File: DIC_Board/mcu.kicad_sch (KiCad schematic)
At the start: 1 part, among them U1 STM32L476ZGTx

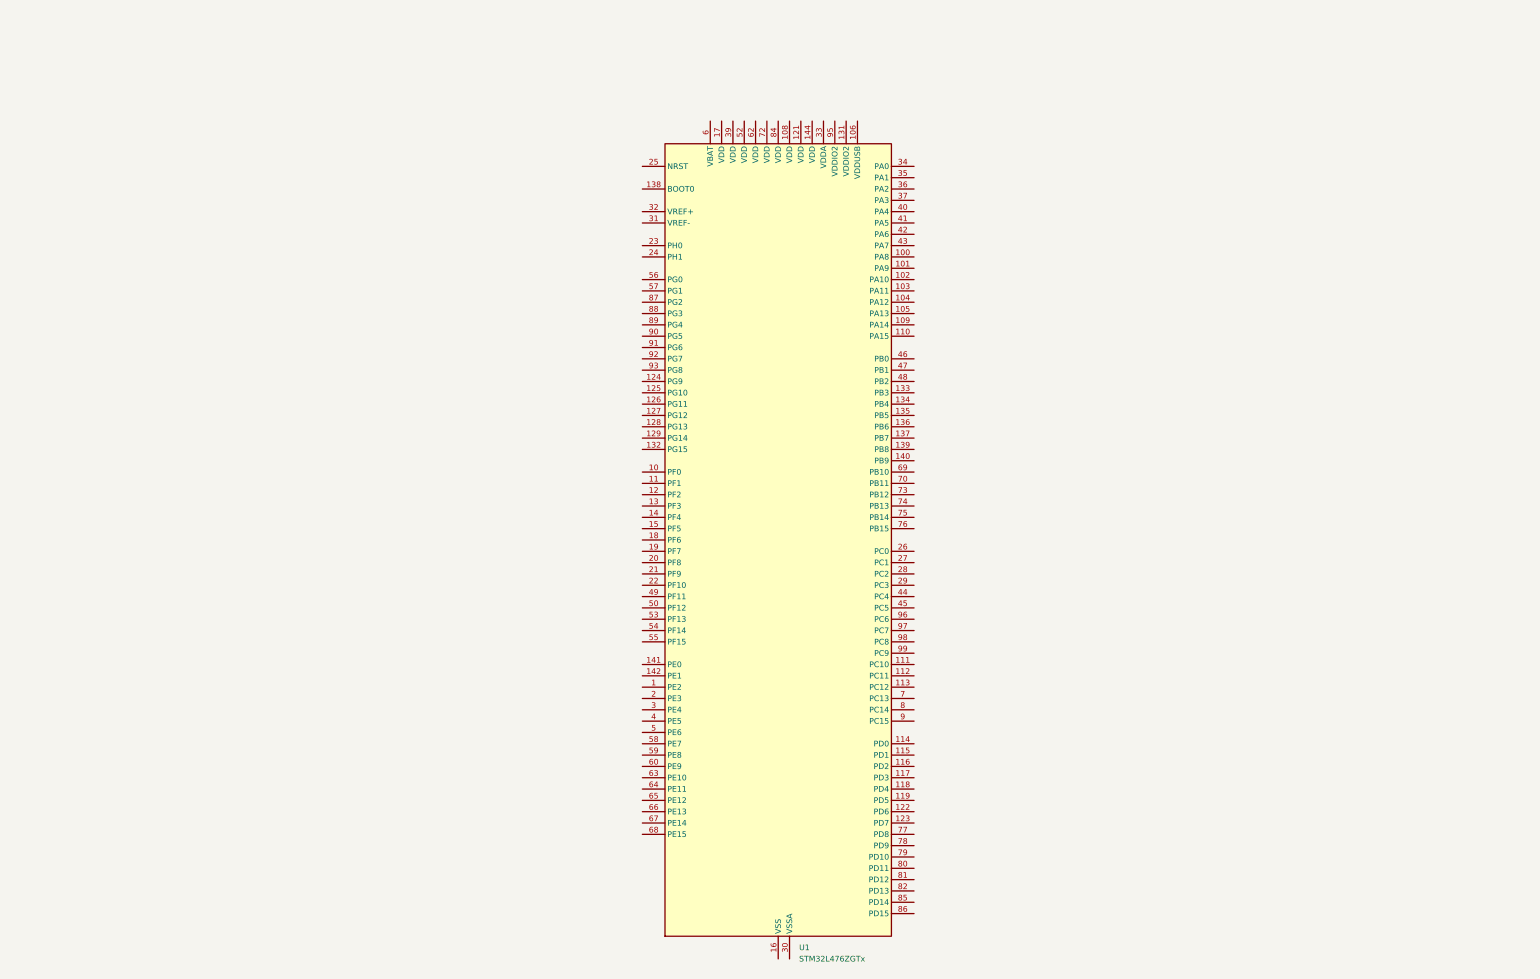
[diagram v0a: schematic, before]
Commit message: Add MCU schematic hierarchy and pin configuration
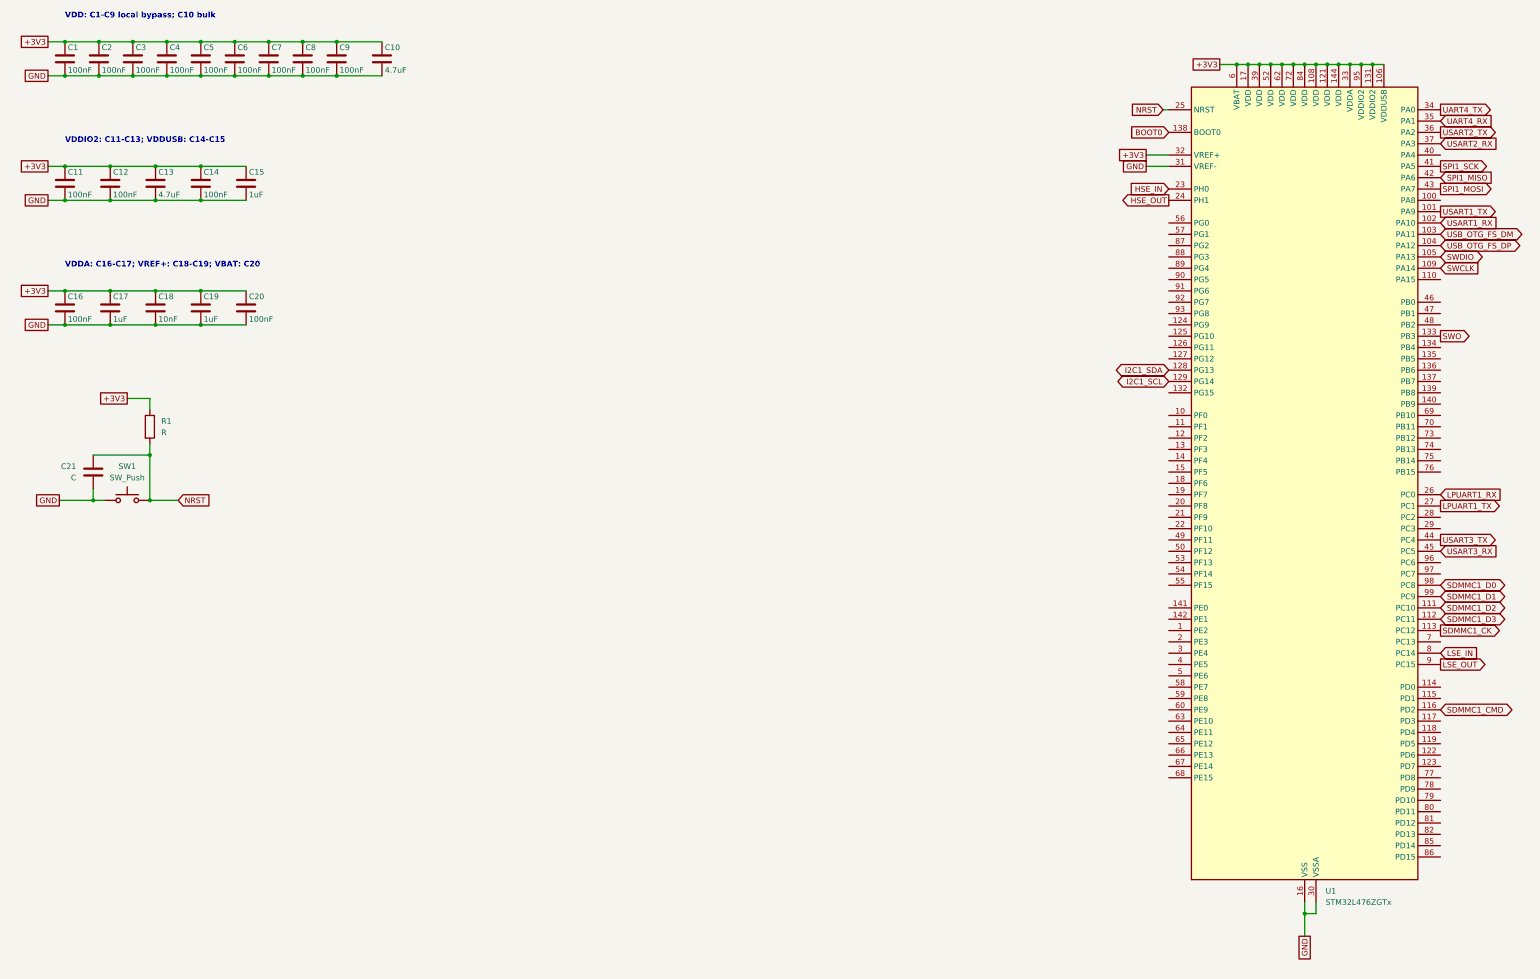
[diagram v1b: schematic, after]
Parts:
- added C1, C11, C12, C14, C16, C2, C20, C3, C4, C5, C6, C7, C8, C9: 100nF, Capacitor_SMD:C_0603_1608Metric, symbol Device:C
- added C10, C13: 4.7uF, Capacitor_SMD:C_0805_2012Metric, symbol Device:C
- added C15, C17, C19: 1uF, Capacitor_SMD:C_0603_1608Metric, symbol Device:C
- added C18: 10nF, Capacitor_SMD:C_0603_1608Metric, symbol Device:C
- added C21: C, symbol Device:C
- added R1: R, symbol Device:R
- added SW1: SW_Push, symbol Switch:SW_Push
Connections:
- net USART1_TX: now reaches U1.101 (PA9)
- net USART1_RX: now reaches U1.102 (PA10)
- net USB_OTG_FS_DM: now reaches U1.103 (PA11)
- net USB_OTG_FS_DP: now reaches U1.104 (PA12)
- net SWDIO: now reaches U1.105 (PA13)
- net +3V3: now reaches U1.106 (VDDUSB)
- net +3V3: now also U1.108 (VDD), U1.121 (VDD), U1.131 (VDDIO2), U1.144 (VDD), U1.17 (VDD), U1.32 (VREF+), U1.33 (VDDA), U1.39 (VDD), U1.52 (VDD), U1.6 (VBAT), U1.62 (VDD), U1.72 (VDD), U1.84 (VDD), U1.95 (VDDIO2), C1.1, C10.1, C11.1, C12.1, C13.1, C14.1, C15.1, C16.1, C17.1, C18.1, C19.1, C2.1, C20.1, C3.1, C4.1, C5.1, C6.1, C7.1, C8.1, C9.1, R1.1
- net GND: now reaches U1.107 (VSS), U1.120 (VSS), U1.130 (VSS), U1.143 (VSS), U1.16 (VSS), U1.38 (VSS), U1.51 (VSS), U1.61 (VSS), U1.71 (VSS), U1.83 (VSS), U1.94 (VSS)
- net GND: now also U1.30 (VSSA), U1.31 (VREF-), C1.2, C10.2, C11.2, C12.2, C13.2, C14.2, C15.2, C16.2, C17.2, C18.2, C19.2, C2.2, C20.2, C21.1, C3.2, C4.2, C5.2, C6.2, C7.2, C8.2, C9.2, SW1.1
- net SWCLK: now reaches U1.109 (PA14)
- net SDMMC1_D2: now reaches U1.111 (PC10)
- net SDMMC1_D3: now reaches U1.112 (PC11)
- net SDMMC1_CK: now reaches U1.113 (PC12)
- net SDMMC1_CMD: now reaches U1.116 (PD2)
- net I2C1_SDA: now reaches U1.128 (PG13)
- net I2C1_SCL: now reaches U1.129 (PG14)
- net SWO: now reaches U1.133 (PB3)
- net BOOT0: now reaches U1.138 (BOOT0)
- net HSE_IN: now reaches U1.23 (PH0)
- net HSE_OUT: now reaches U1.24 (PH1)
- net NRST: now reaches U1.25 (NRST)
- net NRST: now also C21.2, R1.2, SW1.2
- net LPUART1_RX: now reaches U1.26 (PC0)
- net LPUART1_TX: now reaches U1.27 (PC1)
- net UART4_TX: now reaches U1.34 (PA0)
- net UART4_RX: now reaches U1.35 (PA1)
- net USART2_TX: now reaches U1.36 (PA2)
- net USART2_RX: now reaches U1.37 (PA3)
- net SPI1_SCK: now reaches U1.41 (PA5)
- net SPI1_MISO: now reaches U1.42 (PA6)
- net SPI1_MOSI: now reaches U1.43 (PA7)
- net USART3_TX: now reaches U1.44 (PC4)
- net USART3_RX: now reaches U1.45 (PC5)
- net LSE_IN: now reaches U1.8 (PC14)
- net LSE_OUT: now reaches U1.9 (PC15)
- net SDMMC1_D0: now reaches U1.98 (PC8)
- net SDMMC1_D1: now reaches U1.99 (PC9)
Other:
- note added: "VDD: C1-C9 local bypass; C10 bulk"
- note added: "VDDA: C16-C17; VREF+: C18-C19; VBAT: C20"
- note added: "VDDIO2: C11-C13; VDDUSB: C14-C15"
- moved on the sheet: U1

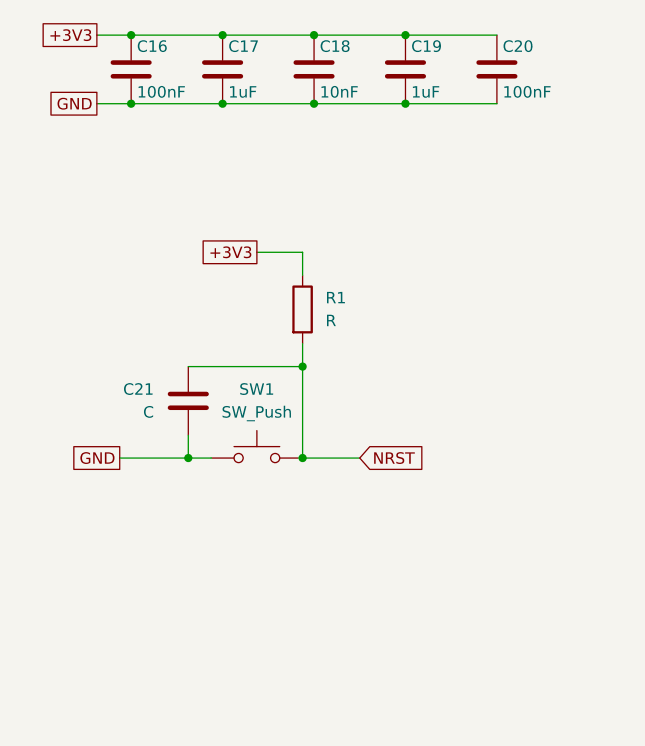
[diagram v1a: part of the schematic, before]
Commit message: Update MCU schematic and add project document
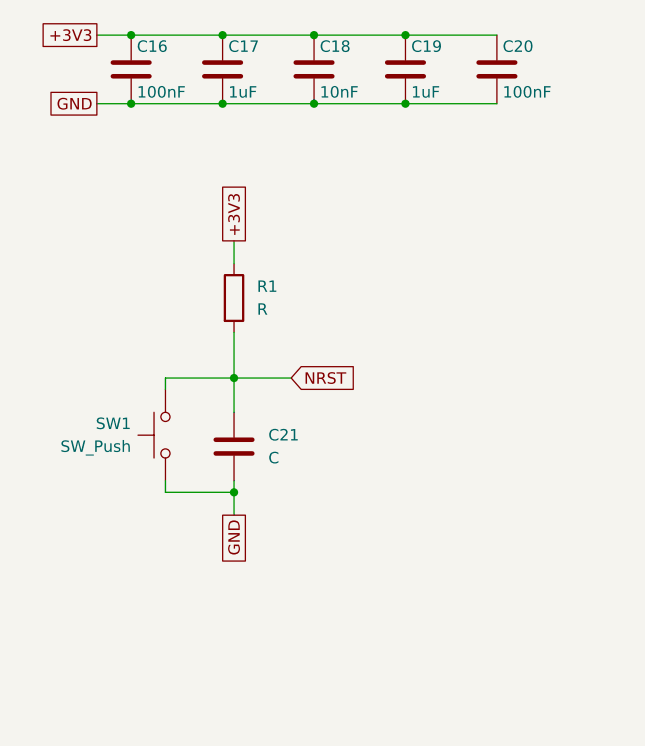
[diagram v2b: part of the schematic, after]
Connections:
- net GND: now also SW1.2; no longer SW1.1
- net NRST: now also SW1.1; no longer SW1.2
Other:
- moved on the sheet: C21, R1, SW1
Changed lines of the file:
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@@
 	)
 	(junction
-		(at 48.26 123.19)
-		(diameter 0)
-		(color 0 0 0 0)
-	)
-	(junction
 		(at 29.21 30.48)
 		(diameter 0)
@@
 	)
 	(junction
-		(at 29.21 38.1)
+		(at 40.64 137.16)
 		(diameter 0)
 		(color 0 0 0 0)
 	)
 	(junction
-		(at 35.56 133.35)
+		(at 29.21 38.1)
 		(diameter 0)
 		(color 0 0 0 0)
 	)
 	(junction
-		(at 48.26 133.35)
+		(at 40.64 124.46)
 		(diameter 0)
 		(color 0 0 0 0)
@@
 	(wire
 		(pts
-			(xy 35.56 130.81) (xy 35.56 133.35)
+			(xy 40.64 135.89) (xy 40.64 137.16)
 		)
 		(stroke
@@
 	(wire
 		(pts
-			(xy 43.18 110.49) (xy 48.26 110.49)
+			(xy 292.1 35.56) (xy 325.12 35.56)
 		)
 		(stroke
@@
 	(wire
 		(pts
-			(xy 292.1 35.56) (xy 325.12 35.56)
+			(xy 40.64 109.22) (xy 40.64 111.76)
 		)
 		(stroke
@@
 	(wire
 		(pts
-			(xy 48.26 110.49) (xy 48.26 113.03)
+			(xy 29.21 66.04) (xy 69.85 66.04)
 		)
 		(stroke
@@
 	(wire
 		(pts
-			(xy 29.21 66.04) (xy 69.85 66.04)
+			(xy 307.34 226.06) (xy 309.88 226.06)
 		)
 		(stroke
@@
 	(wire
 		(pts
-			(xy 307.34 226.06) (xy 309.88 226.06)
+			(xy 33.02 124.46) (xy 40.64 124.46)
 		)
 		(stroke
@@
 	(wire
 		(pts
-			(xy 35.56 123.19) (xy 48.26 123.19)
+			(xy 29.21 58.42) (xy 69.85 58.42)
 		)
 		(stroke
@@
 	(wire
 		(pts
-			(xy 29.21 58.42) (xy 69.85 58.42)
+			(xy 33.02 124.46) (xy 33.02 125.73)
 		)
 		(stroke
@@
 	(wire
 		(pts
-			(xy 29.21 30.48) (xy 100.33 30.48)
+			(xy 33.02 137.16) (xy 40.64 137.16)
 		)
 		(stroke
@@
 	(wire
 		(pts
-			(xy 309.88 226.06) (xy 309.88 223.52)
+			(xy 40.64 137.16) (xy 40.64 139.7)
 		)
 		(stroke
@@
 	(wire
 		(pts
-			(xy 275.59 45.72) (xy 276.86 45.72)
+			(xy 29.21 30.48) (xy 100.33 30.48)
 		)
 		(stroke
@@
 	(wire
 		(pts
-			(xy 25.4 30.48) (xy 29.21 30.48)
+			(xy 40.64 124.46) (xy 40.64 128.27)
 		)
 		(stroke
@@
 	(wire
 		(pts
-			(xy 25.4 38.1) (xy 29.21 38.1)
+			(xy 309.88 226.06) (xy 309.88 223.52)
 		)
 		(stroke
@@
 	(wire
 		(pts
-			(xy 25.4 58.42) (xy 29.21 58.42)
+			(xy 275.59 45.72) (xy 276.86 45.72)
 		)
 		(stroke
@@
 	(wire
 		(pts
-			(xy 25.4 66.04) (xy 29.21 66.04)
+			(xy 25.4 30.48) (xy 29.21 30.48)
 		)
 		(stroke
@@
 	(wire
 		(pts
-			(xy 271.78 58.42) (xy 276.86 58.42)
+			(xy 25.4 38.1) (xy 29.21 38.1)
 		)
 		(stroke
@@
 	(wire
 		(pts
-			(xy 35.56 133.35) (xy 38.1 133.35)
+			(xy 25.4 58.42) (xy 29.21 58.42)
 		)
 		(stroke
@@
 	(wire
 		(pts
-			(xy 25.4 93.98) (xy 29.21 93.98)
+			(xy 25.4 66.04) (xy 29.21 66.04)
 		)
 		(stroke
@@
 	(wire
 		(pts
-			(xy 48.26 133.35) (xy 54.61 133.35)
+			(xy 271.78 58.42) (xy 276.86 58.42)
 		)
 		(stroke
@@
 	(wire
 		(pts
-			(xy 48.26 120.65) (xy 48.26 123.19)
+			(xy 25.4 93.98) (xy 29.21 93.98)
+		)
+		(stroke
+			(width 0)
+			(type default)
+		)
+	)
+	(wire
+		(pts
+			(xy 40.64 124.46) (xy 46.99 124.46)
 		)
 		(stroke
@@
 	(wire
 		(pts
-			(xy 307.34 226.06) (xy 307.34 231.14)
+			(xy 33.02 135.89) (xy 33.02 137.16)
 		)
 		(stroke
@@
 	(wire
 		(pts
-			(xy 27.94 133.35) (xy 35.56 133.35)
+			(xy 307.34 226.06) (xy 307.34 231.14)
 		)
 		(stroke
@@
 	(wire
 		(pts
-			(xy 48.26 123.19) (xy 48.26 133.35)
+			(xy 40.64 119.38) (xy 40.64 124.46)
 		)
 		(stroke
@@
 	(global_label "+3V3"
 		(shape passive)
-		(at 43.18 110.49 180)
+		(at 40.64 109.22 90)
 		(fields_autoplaced yes)
 		(effects
@@
 				(size 1.27 1.27)
 			)
-			(justify right)
+			(justify left)
 		)
 		(property "Intersheetrefs" "${INTERSHEET_REFS}"
-			(at 36.2261 110.49 0)
+			(at 40.64 102.2661 90)
 			(hide yes)
 			(show_name no)
@@
 					(size 1.27 1.27)
 				)
-				(justify right)
+				(justify left)
 			)
 		)
@@
 	(global_label "GND"
 		(shape passive)
-		(at 27.94 133.35 180)
+		(at 40.64 139.7 270)
 		(fields_autoplaced yes)
 		(effects
@@
 		)
 		(property "Intersheetrefs" "${INTERSHEET_REFS}"
-			(at 22.1956 133.35 0)
+			(at 40.64 145.4444 90)
 			(hide yes)
 			(show_name no)
@@
 	(global_label "NRST"
 		(shape input)
-		(at 54.61 133.35 0)
+		(at 46.99 124.46 0)
 		(fields_autoplaced yes)
 		(effects
@@
 		)
 		(property "Intersheetrefs" "${INTERSHEET_REFS}"
-			(at 62.3728 133.35 0)
+			(at 54.7528 124.46 0)
 			(hide yes)
 			(show_name no)
@@
 	(symbol
 		(lib_id "Switch:SW_Push")
-		(at 43.18 133.35 0)
+		(at 33.02 130.81 90)
+		(mirror x)
 		(unit 1)
 		(body_style 1)
@@
 		(in_pos_files yes)
 		(dnp no)
-		(fields_autoplaced yes)
 		(property "Reference" "SW1"
-			(at 43.18 125.73 0)
+			(at 29.21 129.5399 90)
 			(show_name no)
 			(do_not_autoplace no)
@@
 					(size 1.27 1.27)
 				)
+				(justify left)
 			)
 		)
 		(property "Value" "SW_Push"
-			(at 43.18 128.27 0)
+			(at 29.21 132.0799 90)
 			(show_name no)
 			(do_not_autoplace no)
@@
 					(size 1.27 1.27)
 				)
+				(justify left)
 			)
 		)
 		(property "Footprint" ""
-			(at 43.18 128.27 0)
+			(at 27.94 130.81 0)
 			(hide yes)
 			(show_name no)
@@
 		)
 		(property "Datasheet" ""
-			(at 43.18 128.27 0)
+			(at 27.94 130.81 0)
 			(hide yes)
 			(show_name no)
@@
 		)
 		(property "Description" "Push button switch, generic, two pins"
-			(at 43.18 133.35 0)
+			(at 33.02 130.81 0)
 			(hide yes)
 			(show_name no)
@@
 	(symbol
 		(lib_id "Device:C")
-		(at 35.56 127 0)
-		(mirror x)
+		(at 40.64 132.08 180)
 		(unit 1)
 		(body_style 1)
@@
 		(dnp no)
 		(property "Reference" "C21"
-			(at 31.75 125.7299 0)
+			(at 44.45 130.8099 0)
 			(show_name no)
 			(do_not_autoplace no)
@@
 		)
 		(property "Value" "C"
-			(at 31.75 128.2699 0)
+			(at 44.45 133.3499 0)
 			(show_name no)
 			(do_not_autoplace no)
@@
 		)
 		(property "Footprint" ""
-			(at 36.5252 123.19 0)
+			(at 39.6748 128.27 0)
 			(hide yes)
 			(show_name no)
@@
 		)
 		(property "Datasheet" ""
-			(at 35.56 127 0)
+			(at 40.64 132.08 0)
 			(hide yes)
 			(show_name no)
@@
 		)
 		(property "Description" "Unpolarized capacitor"
-			(at 35.56 127 0)
+			(at 40.64 132.08 0)
 			(hide yes)
 			(show_name no)
@@
 	(symbol
 		(lib_id "Device:R")
-		(at 48.26 116.84 0)
+		(at 40.64 115.57 0)
 		(unit 1)
 		(body_style 1)
@@
 		(fields_autoplaced yes)
 		(property "Reference" "R1"
-			(at 50.8 115.5699 0)
+			(at 43.18 114.2999 0)
 			(show_name no)
 			(do_not_autoplace no)
@@
 		)
 		(property "Value" "R"
-			(at 50.8 118.1099 0)
+			(at 43.18 116.8399 0)
 			(show_name no)
 			(do_not_autoplace no)
@@
 		)
 		(property "Footprint" ""
-			(at 46.482 116.84 90)
+			(at 38.862 115.57 90)
 			(hide yes)
 			(show_name no)
@@
 		)
 		(property "Datasheet" ""
-			(at 48.26 116.84 0)
+			(at 40.64 115.57 0)
 			(hide yes)
 			(show_name no)
@@
 		)
 		(property "Description" "Resistor"
-			(at 48.26 116.84 0)
+			(at 40.64 115.57 0)
 			(hide yes)
 			(show_name no)

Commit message: Add MCU clock and RTC integration
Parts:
- added BT1: Battery, symbol Device:Battery
- added C22: 10nF, symbol Device:C
- added C23, C24, C25, C26: C, symbol Device:C
- added C27: 100nF, symbol Device:C
- added FB1: (no value), symbol Device:FerriteBead_Small
- added R2, R4: R, symbol Device:R
- added R3: 0R, symbol Device:R
- added R5: 10k, symbol Device:R
- added U2: AB-RTCMC-32.768kHz-EOA9-S3, symbol DIC_Board:AB-RTCMC-32.768kHz-EOA9-S3
- added Y1: ABM8AAIG-8.000MHz-V2R-T3, DIC_Board:ABM8AAIG-2Pin_3.2x2.5mm, symbol DIC_Board:ABM8AAIG-8.000MHz-V2R-T3
- added Y2: ABS06-107-32.768KHZ-T, DIC_Board:ABS06-107-2Pin_2.0x1.2mm, symbol DIC_Board:ABS06-107-32.768KHZ-T
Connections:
- net +3V3: now also C22.2, FB1.2, R5.1, U2.2 (VDD); no longer U1.32 (VREF+)
- net GND: now also BT1.2 (-), C22.1, C23.2, C24.1, C25.2, C26.1, C27.2, R2.2, U2.6 (VSS)
- net SPI1_MISO: now also U2.5 (SDO)
- net SPI1_MOSI: now also U2.10 (SDI)
- net SPI1_SCK: now also U2.4 (SCL)
- net RTC_CE: now reaches U1.40 (PA4)
- net RTC_CE: now also U2.8 (CE)
- net RTC_INT: now reaches U1.46 (PB0)
- net RTC_INT: now also R5.2, U2.7 (~{INT})
- net RTC_CLKOUT: now reaches U1.47 (PB1)
- net RTC_CLKOUT: now also U2.3 (CLKOUT)
- net RTC_CLKOE: now reaches U1.48 (PB2)
- net RTC_CLKOE: now also U2.1 (CLKOE)
- net HSE_IN: no longer names the net of U1.23 (PH0)
- net HSE_IN: now also C23.1, Y1.1
- net HSE_OUT: no longer names the net of U1.24 (PH1)
- net HSE_OUT: now also R4.2
- net LSE_IN: no longer names the net of U1.8 (PC14)
- net LSE_IN: now also C26.2, Y2.2
- net LSE_OUT: no longer names the net of U1.9 (PC15)
- net LSE_OUT: now also C25.1, Y2.1
- new net: C27.1, FB1.1, U1.32 (VREF+)
- new net: R3.2, U2.9 (VBACKUP)
- new net: BT1.1 (+), R2.1, R3.1
- new net: C24.2, R4.1, Y1.2
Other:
- note added: "DECOUPLING CAPACITORS"
- note added: "MCU"
- note added: "RTC"
- moved on the sheet: C1, C10, C11, C12, C13, C14, C15, C16, C17, C18, C19, C2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

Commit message: Add PSRAM and SD card MCU circuits
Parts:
- added BOOT_SEL: Conn_01x03_Pin, symbol Connector:Conn_01x03_Pin
- added C28, C30: 100nF, Capacitor_SMD:C_0603_1608Metric, symbol Device:C
- added C29: 1uF, Capacitor_SMD:C_0603_1608Metric, symbol Device:C
- added C31: 10uF, Capacitor_SMD:C_0805_2012Metric, symbol Device:C
- added J1: DM3AT-SF-PEJM5, Connector_Card:microSD_HC_Hirose_DM3AT-SF-PEJM5, symbol Connector:Micro_SD_Card_Det_Hirose_DM3AT
- added J2: Conn_ARM_JTAG_SWD_10, symbol Connector:Conn_ARM_JTAG_SWD_10
- added R10, R11, R12, R13, R9: 47K, Resistor_SMD:R_0603_1608Metric, symbol Device:R
- added R14: 10k, symbol Device:R
- added R15, R16, R17, R18: 22R, symbol Device:R
- added R19: 470R, symbol Device:R
- added R6, R8: 10k, Resistor_SMD:R_0603_1608Metric, symbol Device:R
- added R7: 33R, Resistor_SMD:R_0603_1608Metric, symbol Device:R
- added U3: APS6404L-3SQRX-SN, Package_SO:SOIC-8_3.9x4.9mm_P1.27mm, symbol Memory_RAM:APS6404L-3SQRx-SN
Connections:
- net +3V3: now also BOOT_SEL.3 (Pin_3), C28.1, C29.1, C30.1, C31.1, J1.4 (VDD), R10.2, R11.2, R12.2, R13.2, R19.1, R6.2, R8.2, R9.2, U3.8 (VDD)
- net BOOT0: now also BOOT_SEL.2 (Pin_2), R14.1
- net GND: now also BOOT_SEL.1 (Pin_1), C28.2, C29.2, C30.2, C31.2, J1.6 (VSS), J1.9 (DET_B), J1.SH (SHIELD), J2.3 (GND), J2.5 (GND), J2.9 (GNDDetect), R14.2, U3.4 (VSS)
- net NRST: now also R15.2
- net SDMMC1_CK: now also R7.1
- net SDMMC1_CMD: now also J1.3 (CMD), R13.1
- net SDMMC1_D0: now also J1.7 (DAT0), R9.1
- net SDMMC1_D1: now also J1.8 (DAT1), R10.1
- net SDMMC1_D2: now also J1.1 (DAT2), R11.1
- net SDMMC1_D3: now also J1.2 (DAT3/CD), R12.1
- net SWCLK: now also R16.2
- net SWDIO: now also R17.2
- net SWO: now also R18.2
- net QUADSPI_CLK: now reaches U1.63 (PE10)
- net QUADSPI_CLK: now also U3.6 (SCLK)
- net QUADSPI_NCS: now reaches U1.64 (PE11)
- net QUADSPI_NCS: now also R6.1, U3.1 (~{CE})
- net QUADSPI_IO0: now reaches U1.65 (PE12)
- net QUADSPI_IO0: now also U3.5 (SI/SIO0)
- net QUADSPI_IO1: now reaches U1.66 (PE13)
- net QUADSPI_IO1: now also U3.2 (SO/SIO1)
- net QUADSPI_IO2: now reaches U1.67 (PE14)
- net QUADSPI_IO2: now also U3.3 (SIO2)
- net QUADSPI_IO3: now reaches U1.68 (PE15)
- net QUADSPI_IO3: now also U3.7 (SIO3)
- net SD_CARD_DETECT_N: now reaches U1.7 (PC13)
- net SD_CARD_DETECT_N: now also J1.10 (DET_A), R8.1
- new net: J2.6 (SWO/TDO), R18.1
- new net: J2.10 (~{RESET}), R15.1
- new net: J2.1 (VTref), R19.2
- new net: J2.2 (SWDIO/TMS), R17.1
- new net: J2.4 (SWCLK/TCK), R16.1
- new net: J1.5 (CLK), R7.2
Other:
- note added: "8 MiB QUAD-SPI PSRAM"
- note added: "SD CARD"
- note added: "U3: APS6404L-3SQRX-SN; 3.3 V; -40..+105 C"
- moved on the sheet: BT1, C1, C10, C11, C12, C13, C14, C15, C16, C17, C18, C19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

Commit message: Complete MCU and regulated power schematics
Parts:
- C21: value C -> 2.2nF
- C23, C24: value C -> 12pF
- C25, C26: value C -> 6.8pF
- R1: value R -> 47k
- R2: value R -> 10k
- R3: value 0R -> 470R
- R4: value R -> 0R
- renumbered BOOT_SEL to JP1
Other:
- note added: "DEBUG"
- note added: "RESET/BOOT"
- moved on the sheet: C21, J2, JP1, R1, R14, R15, R16, R17, R18, R19, R8, SW1

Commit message: minor changes
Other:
- note removed: "U3: APS6404L-3SQRX-SN; 3.3 V; -40..+105 C"
- moved on the sheet: C16, C17, C18, C19, C20
